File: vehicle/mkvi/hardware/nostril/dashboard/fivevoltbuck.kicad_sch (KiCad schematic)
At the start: 17 parts, among them U1 TPS560430YF

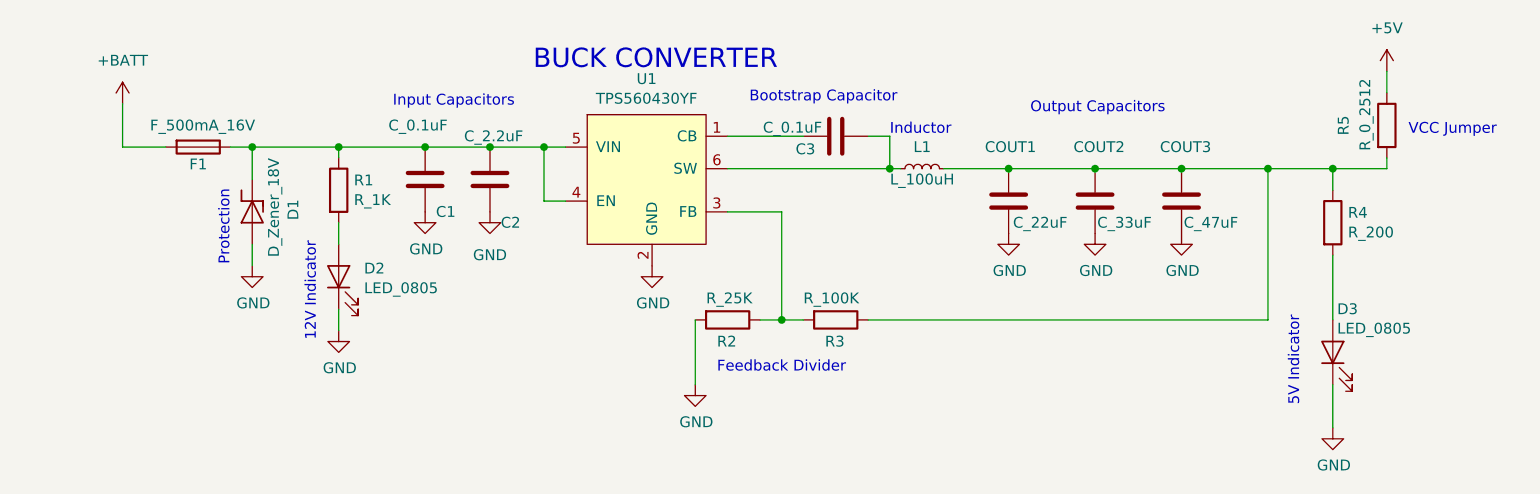
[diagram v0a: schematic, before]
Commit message: Incorporated feedback for dashboard schematic, reorganized top level for organization
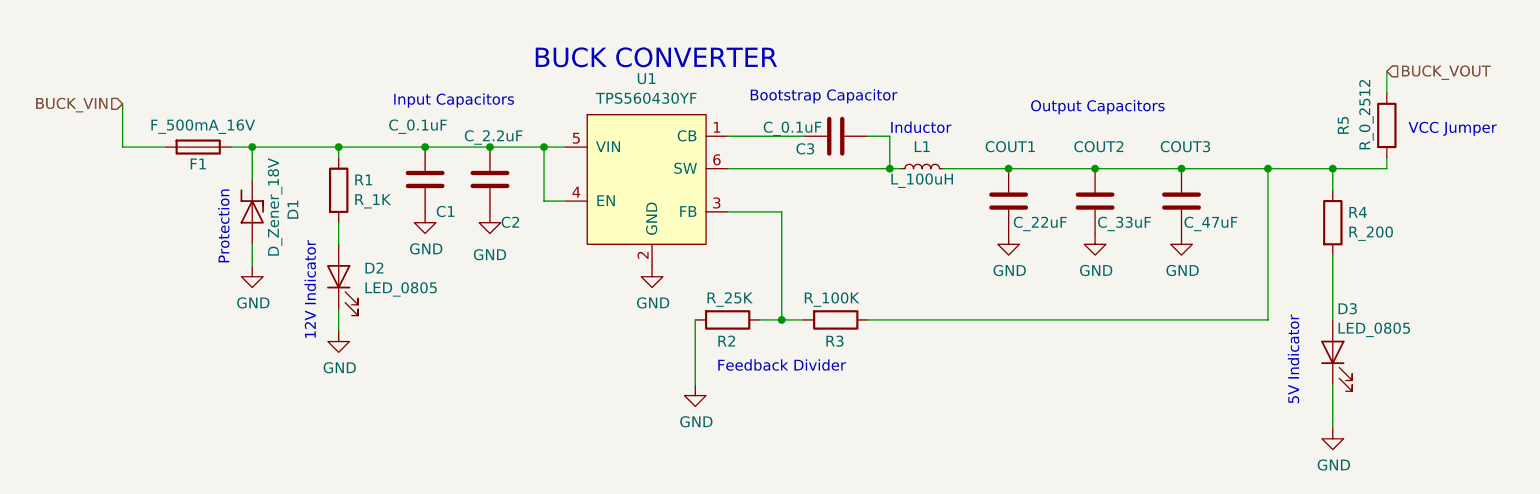
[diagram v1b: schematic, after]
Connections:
- net +5V renamed BUCK_VOUT
- net +BATT renamed BUCK_VIN
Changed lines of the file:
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@@
     (effects (font (size 1.27 1.27)) (justify left bottom))
+  )
+  (hierarchical_label "BUCK_VIN" (shape input) (at 73.66 86.36 180)
+    (effects (font (size 1.27 1.27)) (justify right))
+  )
+  (hierarchical_label "BUCK_VOUT" (shape input) (at 222.25 82.55 0)
+    (effects (font (size 1.27 1.27)) (justify left))
   )
   (symbol (lib_id "formula:R_0_2512") (at 222.25 88.9 0) (unit 1)
@@
     (pin "1")
     (pin "2")
-  )
-  (symbol (lib_id "power:+5V") (at 222.25 82.55 0) (unit 1)
-    (in_bom yes) (on_board yes) (fields_autoplaced)
-    (property "Reference" "#PWR?" (id 0) (at 222.25 86.36 0)
-      (effects (font (size 1.27 1.27)) hide)
-    )
-    (property "Value" "+5V" (id 1) (at 222.25 77.47 0))
-    (property "Footprint" "" (id 2) (at 222.25 82.55 0)
-      (effects (font (size 1.27 1.27)) hide)
-    )
-    (property "Datasheet" "" (id 3) (at 222.25 82.55 0)
-      (effects (font (size 1.27 1.27)) hide)
-    )
-    (pin "1")
   )
   (symbol (lib_id "formula:C_22uF") (at 177.8 97.79 0) (unit 1)
@@
       (effects (font (size 1.27 1.27)) hide)
     )
-    (pin "1")
-  )
-  (symbol (lib_id "power:+BATT") (at 73.66 86.36 0) (unit 1)
-    (in_bom yes) (on_board yes) (fields_autoplaced)
-    (property "Reference" "#PWR?" (id 0) (at 73.66 90.17 0)
-      (effects (font (size 1.27 1.27)) hide)
-    )
-    (property "Value" "+BATT" (id 1) (at 73.66 81.28 0))
-    (property "Footprint" "" (id 2) (at 73.66 86.36 0)
-      (effects (font (size 1.27 1.27)) hide)
-    )
-    (property "Datasheet" "" (id 3) (at 73.66 86.36 0)
-      (effects (font (size 1.27 1.27)) hide)
-    )

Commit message: migrating caps
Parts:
- C1, C3: value C_0.1uF -> 0.1uF; symbol formula:C_0.1uF -> OEM:0.1uF
- C2: footprint footprints:C_0603_1608Metric -> OEM:C_0603
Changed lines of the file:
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@@
     (pin "1")
   )
-  (symbol (lib_id "formula:C_0.1uF") (at 157.48 90.17 90) (unit 1)
+  (symbol (lib_id "OEM:0.1uF") (at 157.48 90.17 90) (unit 1)
     (in_bom yes) (on_board yes)
     (property "Reference" "C3" (id 0) (at 153.924 91.694 90))
-    (property "Value" "C_0.1uF" (id 1) (at 152.4 89.154 90))
+    (property "Value" "0.1uF" (id 1) (at 152.4 89.154 90))
     (property "Footprint" "footprints:C_0805_OEM" (id 2) (at 161.29 89.2048 0)
       (effects (font (size 1.27 1.27)) hide)
@@
       (effects (font (size 1.27 1.27)) (justify left))
     )
-    (property "Footprint" "footprints:C_0603_1608Metric" (id 2) (at 117.8052 100.33 0)
+    (property "Footprint" "OEM:C_0603" (id 2) (at 117.8052 100.33 0)
       (effects (font (size 1.27 1.27)) hide)
     )
@@
     (pin "2")
   )
-  (symbol (lib_id "formula:C_0.1uF") (at 109.22 95.25 0) (unit 1)
+  (symbol (lib_id "OEM:0.1uF") (at 109.22 95.25 0) (unit 1)
     (in_bom yes) (on_board yes)
     (property "Reference" "C1" (id 0) (at 110.49 99.06 0)
       (effects (font (size 1.27 1.27)) (justify left))
     )
-    (property "Value" "C_0.1uF" (id 1) (at 104.902 88.9 0)
-      (effects (font (size 1.27 1.27)) (justify left))
-    )
+    (property "Value" "0.1uF" (id 1) (at 104.902 88.9 0)
+      (effects (font (size 1.27 1.27)) (justify left))
+    )

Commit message: switch micros and leds and adbms
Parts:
- D2, D3: symbol formula:LED_0805 -> OEM:LED_ORANGE
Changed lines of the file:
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@@
     (pin "2")
   )
-  (symbol (lib_id "formula:LED_0805") (at 215.9 115.57 90) (unit 1)
+  (symbol (lib_id "OEM:LED_ORANGE") (at 215.9 115.57 90) (unit 1)
     (in_bom yes) (on_board yes)
     (property "Reference" "D3" (id 0) (at 216.408 110.49 90)
@@
     (pin "1")
   )
-  (symbol (lib_id "formula:LED_0805") (at 99.06 106.68 90) (unit 1)
+  (symbol (lib_id "OEM:LED_ORANGE") (at 99.06 106.68 90) (unit 1)
     (in_bom yes) (on_board yes)
     (property "Reference" "D2" (id 0) (at 102.0318 105.7148 90)

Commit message: switch some resistors over
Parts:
- R1: symbol formula:R_1K -> OEM:1KR
- R3: symbol formula:R_100K -> OEM:100KR
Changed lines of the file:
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@@
     (pin "1")
   )
-  (symbol (lib_id "formula:R_100K") (at 157.48 111.76 270) (unit 1)
+  (symbol (lib_id "OEM:100KR") (at 157.48 111.76 270) (unit 1)
     (in_bom yes) (on_board yes)
     (property "Reference" "R3" (id 0) (at 156.21 114.3 90)
@@
     (pin "2")
   )
-  (symbol (lib_id "formula:R_1K") (at 99.06 96.52 0) (unit 1)
+  (symbol (lib_id "OEM:1KR") (at 99.06 96.52 0) (unit 1)
     (in_bom yes) (on_board yes)
     (property "Reference" "R1" (id 0) (at 100.838 95.3516 0)
